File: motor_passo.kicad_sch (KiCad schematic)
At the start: 83 parts, among them J2 Conn_01x04_Pin, J3 Conn_01x04_Pin, J4 Conn_01x04_Pin, J5 Conn_01x04_Pin, U4 TMC2209-LA, U5 TMC2209-LA, U6 TMC2209-LA, U7 TMC2209-LA

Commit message: 10082026/B
nova revisão
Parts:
- removed R22, R23, R24, R25, R32, R33, R35, R36: 100k, symbol Device:R
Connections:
- net +3V3: now also U5.9 (MS1/AD0), U6.10 (MS2/AD1), U7.10 (MS2/AD1), U7.9 (MS1/AD0); no longer R26.1, R27.1, R34.1, R37.1
- net GND: now also U4.10 (MS2/AD1), U4.9 (MS1/AD0), U5.10 (MS2/AD1), U6.9 (MS1/AD0)
- new net TMC_EN: R26.1, R27.1, R34.1, R37.1
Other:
- note added: "3.4 Configuration Pins(página 14)"
- note added: "UART Address"
- note added: "https://www.analog.com/media/en/technical-documentation/data-sheets/TMC2209_datasheet_rev1.09.pdf"
- note added: "ms1, ms2"
- note added: "os resisto de bra e brb nessa pcb sao de 100mΩ(0.1Ω) e adequaldo para 1.9A(rms) segundo a tabela do datasheet(página 52 8 Selecting Sense Resistors)"
- note added: "se o "TMC_EN" tiver em high(3v3) os pinos 'oax e obx"(oa1, ob1 etc) sai do "Z"(alta impedancia nem low nem high)"
- company: (none) -> ---

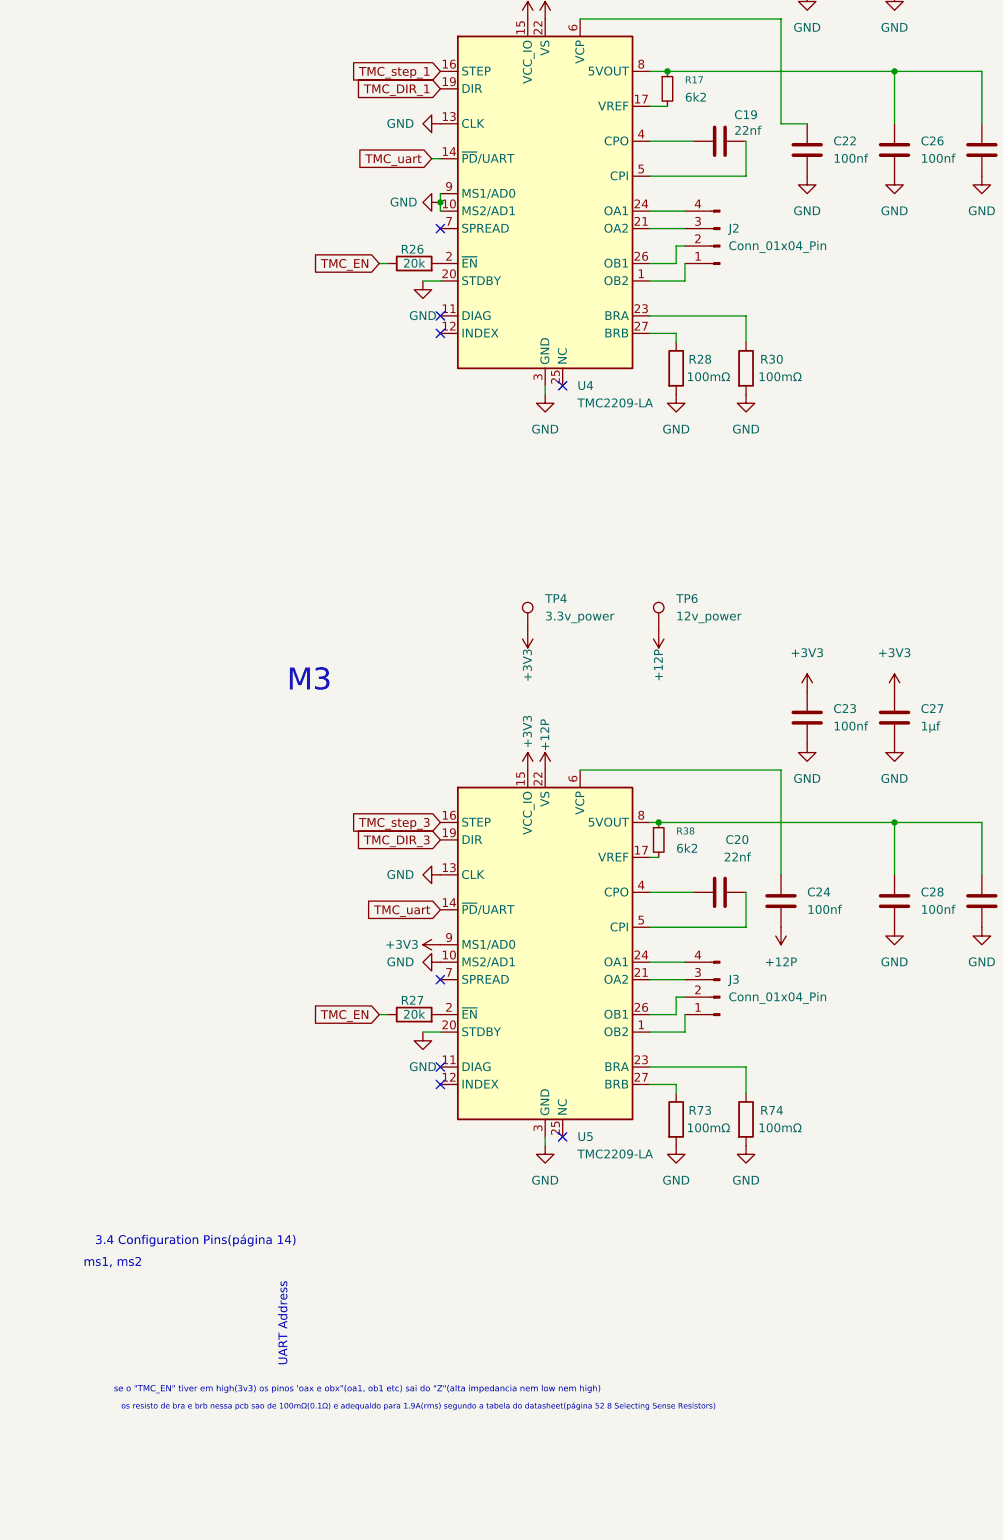
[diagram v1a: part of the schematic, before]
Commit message: 17082026/E
modulo FRAM e Melhoria no esquemático
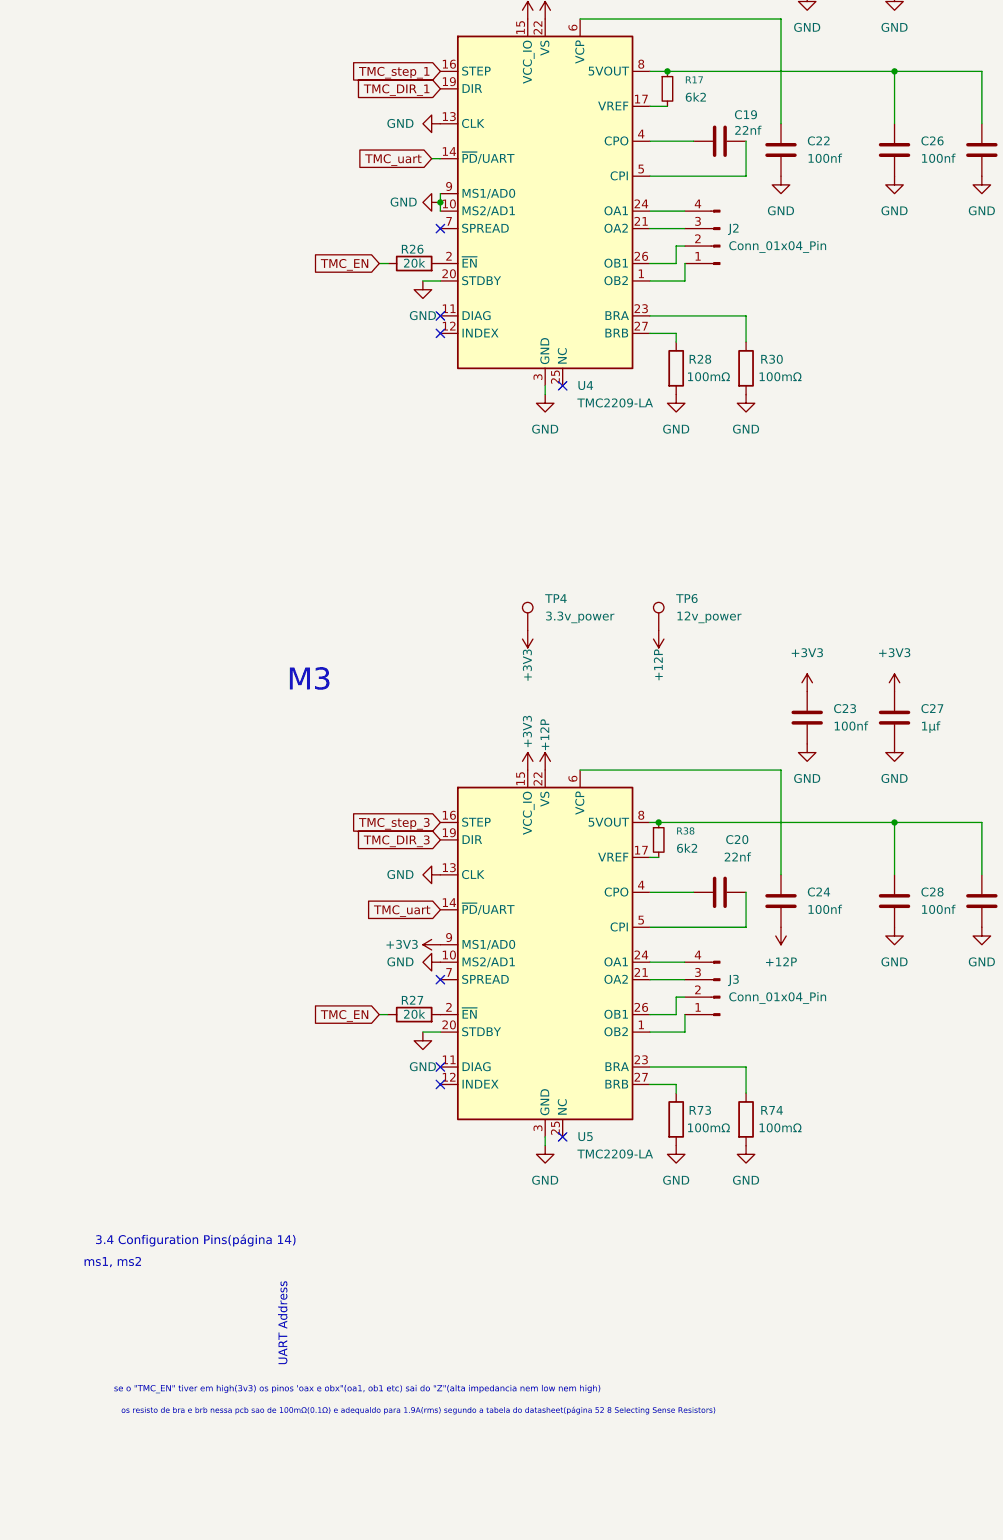
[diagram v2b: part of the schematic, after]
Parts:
- C18: footprint (none) -> Capacitor_SMD:C_0603_1608Metric; jlc_pcb: (none) -> C346191
- C19, C20, C39, C40: footprint (none) -> Capacitor_SMD:C_0603_1608Metric_Pad1.08x0.95mm_HandSolder; jlc_pcb: (none) -> C21122
- C25, C27, C45, C47: footprint (none) -> Capacitor_SMD:C_0805_2012Metric_Pad1.18x1.45mm_HandSolder; jlc_pcb: (none) -> C28323
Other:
- moved on the sheet: C22
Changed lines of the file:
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@@
 	(text "os resisto de bra e brb nessa pcb sao de 100mΩ(0.1Ω) e adequaldo para 1.9A(rms) segundo a tabela do datasheet(página 52 8 Selecting Sense Resistors)"
 		(exclude_from_sim no)
-		(at 62.865 261.62 0)
+		(at 62.865 262.255 0)
 		(effects
 			(font
@@
 	(wire
 		(pts
-			(xy 115.57 74.93) (xy 119.38 74.93)
-		)
-		(stroke
-			(width 0)
-			(type default)
-			(color 255 153 0 1)
-		)
-	)
-	(wire
-		(pts
 			(xy 267.97 184.15) (xy 274.32 184.15)
 		)
@@
 		)
 	)
+	(rule_area
+		(exclude_from_sim no)
+		(in_bom yes)
+		(on_board yes)
+		(dnp no)
+		(polyline
+			(pts
+				(xy 13.335 259.715) (xy 13.335 261.62) (xy 13.97 260.985) (xy 111.76 260.985) (xy 111.125 260.35)
+				(xy 13.97 260.35)
+			)
+			(stroke
+				(width 0)
+				(type dash)
+			)
+			(fill
+				(type none)
+			)
+		)
+	)
 	(symbol
 		(lib_id "Connector:TestPoint")
@@
 	(symbol
 		(lib_id "power:GND")
-		(at 119.38 82.55 0)
+		(at 115.57 82.55 0)
 		(unit 1)
 		(body_style 1)
@@
 		(fields_autoplaced yes)
 		(property "Reference" "#PWR063"
-			(at 119.38 88.9 0)
+			(at 115.57 88.9 0)
 			(hide yes)
 			(show_name no)
@@
 		)
 		(property "Value" "GND"
-			(at 119.38 87.63 0)
+			(at 115.57 87.63 0)
 			(show_name no)
 			(do_not_autoplace no)
@@
 		)
 		(property "Footprint" ""
-			(at 119.38 82.55 0)
+			(at 115.57 82.55 0)
 			(hide yes)
 			(show_name no)
@@
 		)
 		(property "Datasheet" ""
-			(at 119.38 82.55 0)
+			(at 115.57 82.55 0)
 			(hide yes)
 			(show_name no)
@@
 		)
 		(property "Description" "Power symbol creates a global label with name \"GND\" , ground"
-			(at 119.38 82.55 0)
+			(at 115.57 82.55 0)
 			(hide yes)
 			(show_name no)
@@
 			)
 		)
-		(property "Footprint" ""
+		(property "Footprint" "Capacitor_SMD:C_0603_1608Metric_Pad1.08x0.95mm_HandSolder"
 			(at 110.49 185.7248 0)
 			(hide yes)
@@
 			)
 		)
+		(property "jlc_pcb:" "C21122"
+			(at 106.68 186.69 90)
+			(hide yes)
+			(show_name no)
+			(do_not_autoplace no)
+			(effects
+				(font
+					(size 1.27 1.27)
+				)
+			)
+		)
 		(pin "2"
 		)
@@
 			)
 		)
-		(property "Footprint" ""
+		(property "Footprint" "Capacitor_SMD:C_0805_2012Metric_Pad1.18x1.45mm_HandSolder"
 			(at 302.5648 154.94 0)
 			(hide yes)
@@
 			)
 		)
+		(property "jlc_pcb:" "C28323"
+			(at 303.53 158.75 0)
+			(hide yes)
+			(show_name no)
+			(do_not_autoplace no)
+			(effects
+				(font
+					(size 1.27 1.27)
+				)
+			)
+		)
 		(pin "2"
 		)
@@
 			)
 		)
-		(property "Footprint" ""
+		(property "Footprint" "Capacitor_SMD:C_0603_1608Metric_Pad1.08x0.95mm_HandSolder"
 			(at 281.94 183.1848 0)
 			(hide yes)
@@
 			)
 		)
+		(property "jlc_pcb:" "C21122"
+			(at 278.13 184.15 90)
+			(hide yes)
+			(show_name no)
+			(do_not_autoplace no)
+			(effects
+				(font
+					(size 1.27 1.27)
+				)
+			)
+		)
 		(pin "2"
 		)
@@
 			)
 		)
-		(property "Footprint" ""
+		(property "Footprint" "Capacitor_SMD:C_0603_1608Metric_Pad1.08x0.95mm_HandSolder"
 			(at 281.94 73.9648 0)
 			(hide yes)
@@
 			)
 		)
+		(property "jlc_pcb:" "C21122"
+			(at 278.13 74.93 90)
+			(hide yes)
+			(show_name no)
+			(do_not_autoplace no)
+			(effects
+				(font
+					(size 1.27 1.27)
+				)
+			)
+		)
 		(pin "2"
 		)
@@
 			)
 		)
-		(property "Footprint" ""
+		(property "Footprint" "Capacitor_SMD:C_0805_2012Metric_Pad1.18x1.45mm_HandSolder"
 			(at 131.1148 48.26 0)
 			(hide yes)
@@
 			)
 		)
+		(property "jlc_pcb:" "C28323"
+			(at 132.08 52.07 0)
+			(hide yes)
+			(show_name no)
+			(do_not_autoplace no)
+			(effects
+				(font
+					(size 1.27 1.27)
+				)
+			)
+		)
 		(pin "2"
 		)
@@
 			)
 		)
-		(property "Footprint" ""
+		(property "Footprint" "Capacitor_SMD:C_0603_1608Metric_Pad1.08x0.95mm_HandSolder"
 			(at 110.49 76.5048 0)
 			(hide yes)
@@
 			)
 		)
+		(property "jlc_pcb:" "C21122"
+			(at 106.68 77.47 90)
+			(hide yes)
+			(show_name no)
+			(do_not_autoplace no)
+			(effects
+				(font
+					(size 1.27 1.27)
+				)
+			)
+		)
 		(pin "2"
 		)
@@
 	(symbol
 		(lib_id "Device:C")
-		(at 119.38 78.74 180)
+		(at 115.57 78.74 180)
 		(unit 1)
 		(body_style 1)
@@
 		(fields_autoplaced yes)
 		(property "Reference" "C22"
-			(at 123.19 77.4699 0)
+			(at 119.38 77.4699 0)
 			(show_name no)
 			(do_not_autoplace no)
@@
 		)
 		(property "Value" "100nf"
-			(at 123.19 80.0099 0)
+			(at 119.38 80.0099 0)
 			(show_name no)
 			(do_not_autoplace no)
@@
 		)
 		(property "Footprint" "Capacitor_SMD:C_0603_1608Metric"
-			(at 118.4148 74.93 0)
+			(at 114.6048 74.93 0)
 			(hide yes)
 			(show_name no)
@@
 		)
 		(property "Datasheet" ""
-			(at 119.38 78.74 0)
+			(at 115.57 78.74 0)
 			(hide yes)
 			(show_name no)
@@
 		)
 		(property "Description" "Unpolarized capacitor"
-			(at 119.38 78.74 0)
+			(at 115.57 78.74 0)
 			(hide yes)
 			(show_name no)
@@
 		)
 		(property "jlc_pcb/lcsc_ID:" "C346191"
-			(at 119.38 78.74 0)
+			(at 115.57 78.74 0)
 			(hide yes)
 			(show_name no)
@@
 		)
 		(property "jlc_pcb:" "C346191"
-			(at 119.38 78.74 0)
+			(at 115.57 78.74 0)
 			(hide yes)
 			(show_name no)
@@
 		)
 		(property "mpn" "CL10B104KB8NFNC"
-			(at 119.38 78.74 0)
+			(at 115.57 78.74 0)
 			(hide yes)
 			(show_name no)
@@
 			)
 		)
-		(property "Footprint" ""
+		(property "Footprint" "Capacitor_SMD:C_0805_2012Metric_Pad1.18x1.45mm_HandSolder"
 			(at 302.5648 45.72 0)
 			(hide yes)
@@
 			)
 		)
+		(property "jlc_pcb:" "C28323"
+			(at 303.53 49.53 0)
+			(hide yes)
+			(show_name no)
+			(do_not_autoplace no)
+			(effects
+				(font
+					(size 1.27 1.27)
+				)
+			)
+		)
 		(pin "2"
 		)
@@
 			)
 		)
-		(property "Footprint" ""
+		(property "Footprint" "Capacitor_SMD:C_0805_2012Metric_Pad1.18x1.45mm_HandSolder"
 			(at 131.1148 157.48 0)
 			(hide yes)
@@
 			)
 		)
+		(property "jlc_pcb:" "C28323"
+			(at 132.08 161.29 0)
+			(hide yes)
+			(show_name no)
+			(do_not_autoplace no)
+			(effects
+				(font
+					(size 1.27 1.27)
+				)
+			)
+		)
 		(pin "2"
 		)
@@
 			)
 		)
-		(property "Footprint" ""
+		(property "Footprint" "Capacitor_SMD:C_0603_1608Metric"
 			(at 42.8752 38.1 0)
 			(hide yes)
@@
 			(at 41.91 34.29 0)
 			(hide yes)
+			(show_name no)
+			(do_not_autoplace no)
+			(effects
+				(font
+					(size 1.27 1.27)
+				)
+			)
+		)
+		(property "jlc_pcb:" "C346191"
+			(at 41.91 34.29 0)
+			(hide yes)

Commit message: 21082026/G
falta muita coisa
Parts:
- renumbered C18 to C13, C96 to C14, C19 to C15, C20 to C16, C22 to C17, C24 to C18, C21 to C19, C23 to C20, C25 to C21, C26 to C22, C27 to C23, C28 to C24, C30 to C25, C32 to C26, C91 to C27, C33 to C28, C34 to C29, C35 to C30, C36 to C31, C37 to C32, C38 to C33, C92 to C34, C39 to C35, C40 to C36, C44 to C37, C41 to C38, C42 to C39, C43 to C40, C45 to C41, C46 to C42, C47 to C43, C48 to C44, C50 to C45, C52 to C46, C53 to C47, C54 to C48, C55 to C49, C56 to C50, C57 to C51, C58 to C52, F7 to F2, F8 to F3, FB1 to FB2, J2 to J3, J3 to J4, J4 to J5, J5 to J6, R26 to R55, R27 to R56, R38 to R57, R17 to R58, R28 to R59, R73 to R60, R30 to R61, R74 to R62, R34 to R63, R37 to R64, R75 to R65, R40 to R66, R39 to R67, R29 to R68, R41 to R69, R31 to R70, TP8 to TP10, TP9 to TP11, TP10 to TP12, TP3 to TP5, TP4 to TP6, TP5 to TP7, TP6 to TP8, TP7 to TP9

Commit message: 29082026/I
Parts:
- removed C32, C33, C51, C52: 100µf, symbol Device:C
- added C32, C33, C51, C52: 100µf, Capacitor_SMD:CP_Elec_6.3x7.7, symbol Device:C_Polarized
- C13: jlc_pcb: C346191 -> C307348; mouser: (none) -> 187-CL10B104KB8WPNC; mpn (none) -> CL10B104KB8WPNC
- C14, C25, C26, C45, C46: footprint (none) -> Capacitor_SMD:C_0603_1608Metric; jlc_pcb: (none) -> C162274; mouser: (none) -> 81-GRM188R61E475KE1D; mpn (none) -> GRM188R61E475KE11D
- C17, C18, C19, C20, C22, C24, C28, C30, C37, C38, C39, C40, C42, C44, C47, C49: jlc_pcb: C346191 -> C307348; mouser: (none) -> 187-CL10B104KB8WPNC; mpn CL10B104KB8NFNC -> CL10B104KB8WPNC
- C29, C31, C48, C50: footprint (none) -> Capacitor_SMD:C_1206_3216Metric_Pad1.33x1.80mm_HandSolder; jlc_pcb: (none) -> C13585; mouser: (none) -> 187-CL31B106KLK6PNE; mpn (none) -> CL31A106KBHNNNE
- R59, R60, R61, R62, R67, R68, R69, R70: footprint Resistor_SMD:R_1206_3216Metric -> Resistor_SMD:R_2512_6332Metric_Pad1.40x3.35mm_HandSolder; jlc_pcb: C309528 -> C844904; mouser: (none) -> 71-WSL2512R1000FEA; mpn PE1206FRF470R1L -> WSL2512R1000FEA
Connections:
- net +12P: now also C32.1, C33.1, C51.1, C52.1
- net GND: now also C32.2, C33.2, C51.2, C52.2

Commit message: o .bom não foi terminado
O desafio e todo custar menos de 150 dólares(eua) e menos de 1000r(reais)
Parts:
- C14, C25, C26, C45, C46: footprint Capacitor_SMD:C_0603_1608Metric -> Capacitor_SMD:C_0603_1608Metric_Pad1.08x0.95mm_HandSolder
- C15, C16, C35, C36: mouser: (none) -> 187-CL10B223KB8NNNC; mpn (none) -> CL10B223KB8NNNC
- C21, C23, C41, C43: mouser: (none) -> 187-CL21B105KBFNNNE; mpn (none) -> CL21B105KBFNNNE
- C27, C34: mouser: (none) -> 232-35YXJ1000M125X20; mpn (none) -> 35YXJ1000M12.5X20
- C32, C33, C51, C52: mouser: (none) -> 232-35TZV100M6.3X8
- TP10, TP11, TP12, TP5, TP6, TP7, TP8, TP9: now left out of the parts list
- U4, U5, U6, U7: mouser: (none) -> 00-TMC2209-LA-T

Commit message: 05092026/00001
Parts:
- R57, R58, R65, R66: jlc_pcb: (none) -> C114535; mouser: (none) -> 603-RC0805FR-076K2L; mpn (none) -> RC0805FR-076K2L
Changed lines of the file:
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@@
 			)
 		)
+		(property "jlc_pcb:" "C114535"
+			(at 270.51 67.31 0)
+			(hide yes)
+			(show_name no)
+			(do_not_autoplace no)
+			(effects
+				(font
+					(size 1.27 1.27)
+				)
+			)
+		)
+		(property "mouser:" "603-RC0805FR-076K2L"
+			(at 270.51 67.31 0)
+			(hide yes)
+			(show_name no)
+			(do_not_autoplace no)
+			(effects
+				(font
+					(size 1.27 1.27)
+				)
+			)
+		)
+		(property "mpn" "RC0805FR-076K2L"
+			(at 270.51 67.31 0)
+			(hide yes)
+			(show_name no)
+			(do_not_autoplace no)
+			(effects
+				(font
+					(size 1.27 1.27)
+				)
+			)
+		)
 		(pin "1"
 		)
@@
 			)
 		)
+		(property "jlc_pcb:" "C114535"
+			(at 270.51 176.53 0)
+			(hide yes)
+			(show_name no)
+			(do_not_autoplace no)
+			(effects
+				(font
+					(size 1.27 1.27)
+				)
+			)
+		)
+		(property "mouser:" "603-RC0805FR-076K2L"
+			(at 270.51 176.53 0)
+			(hide yes)
+			(show_name no)
+			(do_not_autoplace no)
+			(effects
+				(font
+					(size 1.27 1.27)
+				)
+			)
+		)
+		(property "mpn" "RC0805FR-076K2L"
+			(at 270.51 176.53 0)
+			(hide yes)
+			(show_name no)
+			(do_not_autoplace no)
+			(effects
+				(font
+					(size 1.27 1.27)
+				)
+			)
+		)
 		(pin "1"
 		)
@@
 			)
 		)
+		(property "jlc_pcb:" "C114535"
+			(at 97.79 179.07 0)
+			(hide yes)
+			(show_name no)
+			(do_not_autoplace no)
+			(effects
+				(font
+					(size 1.27 1.27)
+				)
+			)
+		)
+		(property "mouser:" "603-RC0805FR-076K2L"
+			(at 97.79 179.07 0)
+			(hide yes)
+			(show_name no)
+			(do_not_autoplace no)
+			(effects
+				(font
+					(size 1.27 1.27)
+				)
+			)
+		)
+		(property "mpn" "RC0805FR-076K2L"
+			(at 97.79 179.07 0)
+			(hide yes)
+			(show_name no)
+			(do_not_autoplace no)
+			(effects
+				(font
+					(size 1.27 1.27)
+				)
+			)
+		)
 		(pin "1"
 		)
@@
 			(at 99.06 69.85 0)
 			(hide yes)
+			(show_name no)
+			(do_not_autoplace no)
+			(effects
+				(font
+					(size 1.27 1.27)
+				)
+			)
+		)
+		(property "jlc_pcb:" "C114535"
+			(at 99.06 69.85 0)
+			(hide yes)
+			(show_name no)
+			(do_not_autoplace no)
+			(effects
+				(font
+					(size 1.27 1.27)
+				)
+			)
+		)
+		(property "mouser:" "603-RC0805FR-076K2L"
+			(at 99.06 69.85 0)
+			(hide yes)
+			(show_name no)
+			(do_not_autoplace no)
+			(effects
+				(font
+					(size 1.27 1.27)
+				)
+			)
+		)
+		(property "mpn" "RC0805FR-076K2L"
+			(at 99.06 69.85 0)
+			(hide yes)

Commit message: 27092026/0002
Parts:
- R55, R56, R63, R64: value 20k -> 10kΩ; footprint (none) -> Resistor_SMD:R_0603_1608Metric Resistor_SMD_R_0603_1608Metric; jlc_pcb: (none) -> C13564; mouser: (none) -> 81-NCP18XH103F03RB; mpn (none) -> NCP18XH103F03RB
- R57, R58, R65, R66: footprint (none) -> Resistor_SMD:R_0805_2012Metric_Pad1.20x1.40mm_HandSolder
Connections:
- net TMC_SPRE_1: now reaches U4.7 (SPREAD)
- net TMC_SPRE_3: now reaches U5.7 (SPREAD)
- net TMC_SPRE_2: now reaches U6.7 (SPREAD)
- net TMC_SPRE_4: now reaches U7.7 (SPREAD)
- no-connect marks 16 -> 12
